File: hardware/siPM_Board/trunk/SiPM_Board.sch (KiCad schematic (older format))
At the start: 25 parts, among them J1 Conn_02x34_Odd_Even, J2 Conn_02x34_Odd_Even, U1 LM94021, U2 S14161-6050HS-04, U3 S14161-6050HS-04, U4 S14161-6050HS-04, U5 S14161-6050HS-04

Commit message: All footprints are made
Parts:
- J1, J2: footprint Connector_Samtec_HLE_SMD:Samtec_HLE-134-02-xxx-DV-BE-A_2x34_P2.54mm_Horizontal -> Arich_SiPM_Footprints:MW-34-03-G-D-245-065-ES
- U1: footprint (none) -> Arich_SiPM_Footprints:Texas_R-PDSO-G6
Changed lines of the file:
@@
 F 0 "U1" H 2150 4085 50  0000 C CNN
 F 1 "LM94021" H 2150 4176 50  0000 C CNN
-F 2 "" H 2195 4473 50  0001 C CNN
+F 2 "Arich_SiPM_Footprints:Texas_R-PDSO-G6" H 2195 4473 50  0001 C CNN
 F 3 "https://www.ti.com/lit/ds/symlink/lm94021.pdf?ts=1612369710364&ref_url=https%253A%252F%252Fwww.ti.com%252Fproduct%252FLM94021" H 2195 4473 50  0001 C CNN
 	1    2150 4650
@@
 F 0 "J1" H 5650 1525 50  0000 R CNN
 F 1 "Conn_02x34_Odd_Even" H 6400 1650 50  0000 R CNN
-F 2 "Connector_Samtec_HLE_SMD:Samtec_HLE-134-02-xxx-DV-BE-A_2x34_P2.54mm_Horizontal" H 6000 3550 50  0001 C CNN
+F 2 "Arich_SiPM_Footprints:MW-34-03-G-D-245-065-ES" H 6000 3550 50  0001 C CNN
 F 3 "~" H 6000 3550 50  0001 C CNN
 	1    6000 3550
@@
 F 0 "J2" H 8975 1525 50  0000 R CNN
 F 1 "Conn_02x34_Odd_Even" H 9750 1650 50  0000 R CNN
-F 2 "Connector_Samtec_HLE_SMD:Samtec_HLE-134-02-xxx-DV-BE-A_2x34_P2.54mm_Horizontal" H 9350 3550 50  0001 C CNN
+F 2 "Arich_SiPM_Footprints:MW-34-03-G-D-245-065-ES" H 9350 3550 50  0001 C CNN
 F 3 "~" H 9350 3550 50  0001 C CNN
 	1    9350 3550

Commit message: Layout Needs Editing
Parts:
- C1, C10, C11, C12, C13, C14, C15, C16, C17, C18, C2, C3, C4, C5, C6, C7, C8, C9: footprint Capacitor_SMD:C_1206_3216Metric_Pad1.33x1.80mm_HandSolder -> Capacitor_SMD:C_0603_1608Metric_Pad1.08x0.95mm_HandSolder; Item Cost $0.85 -> $0.12; MFN C3216C0G2A104J160AC -> 0603B104K101CT; Supplier P/N 445-172677-1-ND -> 1292-1392-1-ND

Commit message: Schematic changes made
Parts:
- removed C10, C11, C14, C15, C16, C5, C6, C9: 100nF, Capacitor_SMD:C_0603_1608Metric_Pad1.08x0.95mm_HandSolder, symbol Device:C
- renumbered C18 to C10, C12 to C5, C13 to C6, C17 to C9
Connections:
- net BIAS1: now also J1.2 (Pin_2); no longer C3.1, C4.1, C7.1, C8.1, J1.67 (Pin_67), J1.68 (Pin_68), U3.B1 (A1K), U3.B3 (A2K), U3.B5 (A3K), U3.B7 (A4K), U3.D1 (B1K), U3.D3 (B2K), U3.D5 (B3K), U3.D7 (B4K), U3.F2 (C1K), U3.F4 (C2K), U3.F6 (C3K), U3.F8 (C4K), U3.H2 (D1K), U3.H4 (D2K), U3.H6 (D3K), U3.H8 (D4K)
- net BIAS2: now also C3.1, C4.1, J1.67 (Pin_67), U3.B1 (A1K), U3.B3 (A2K), U3.B5 (A3K), U3.B7 (A4K), U3.D1 (B1K), U3.D3 (B2K), U3.D5 (B3K), U3.D7 (B4K), U3.F2 (C1K), U3.F4 (C2K), U3.F6 (C3K), U3.F8 (C4K), U3.H2 (D1K), U3.H4 (D2K), U3.H6 (D3K), U3.H8 (D4K); no longer C5.1, C6.1, J2.67 (Pin_67), J2.68 (Pin_68), U4.B1 (A1K), U4.B3 (A2K), U4.B5 (A3K), U4.B7 (A4K), U4.D1 (B1K), U4.D3 (B2K), U4.D5 (B3K), U4.D7 (B4K), U4.F2 (C1K), U4.F4 (C2K), U4.F6 (C3K), U4.F8 (C4K), U4.H2 (D1K), U4.H4 (D2K), U4.H6 (D3K), U4.H8 (D4K), U5.B1 (A1K), U5.B3 (A2K), U5.B5 (A3K), U5.B7 (A4K), U5.D1 (B1K), U5.D3 (B2K), U5.D5 (B3K), U5.D7 (B4K), U5.F2 (C1K), U5.F4 (C2K), U5.F6 (C3K), U5.F8 (C4K), U5.H2 (D1K), U5.H4 (D2K), U5.H6 (D3K), U5.H8 (D4K)
- net GND: now also J1.66 (Pin_66), J2.66 (Pin_66); no longer C7.2, C8.2, J1.2 (Pin_2), J2.2 (Pin_2)
- net OUT: now also J1.68 (Pin_68); no longer J1.66 (Pin_66)
- new net: C7.2, C8.2
- new net BIAS3: C5.1, C6.1, J2.2 (Pin_2), U4.B1 (A1K), U4.B3 (A2K), U4.B5 (A3K), U4.B7 (A4K), U4.D1 (B1K), U4.D3 (B2K), U4.D5 (B3K), U4.D7 (B4K), U4.F2 (C1K), U4.F4 (C2K), U4.F6 (C3K), U4.F8 (C4K), U4.H2 (D1K), U4.H4 (D2K), U4.H6 (D3K), U4.H8 (D4K)
- new net BIAS4: C7.1, C8.1, J2.67 (Pin_67), J2.68 (Pin_68), U5.B1 (A1K), U5.B3 (A2K), U5.B5 (A3K), U5.B7 (A4K), U5.D1 (B1K), U5.D3 (B2K), U5.D5 (B3K), U5.D7 (B4K), U5.F2 (C1K), U5.F4 (C2K), U5.F6 (C3K), U5.F8 (C4K), U5.H2 (D1K), U5.H4 (D2K), U5.H6 (D3K), U5.H8 (D4K)
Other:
- moved on the sheet: C10, C5, C6, C9, J1, J2, U1, U2, U3, U4, U5

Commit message: Tracing incomplete
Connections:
- net GND: now also C7.2, C8.2
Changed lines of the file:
@@
 Text Label 9850 1850 2    50   ~ 0
 BIAS3
+$Comp
+L power:GND #PWR?
+U 1 1 602B2E79
+P 6550 4150
+F 0 "#PWR?" H 6550 3900 50  0001 C CNN
+F 1 "GND" H 6555 3977 50  0000 C CNN
+F 2 "" H 6550 4150 50  0001 C CNN
+F 3 "" H 6550 4150 50  0001 C CNN
+	1    6550 4150
+	1    0    0    -1
+$EndComp
 $EndSCHEMATC

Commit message: Tracing incomplete
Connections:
- net BIAS2: now also J1.68 (Pin_68); no longer J1.67 (Pin_67)
- net OUT: now also J1.67 (Pin_67); no longer J1.68 (Pin_68)
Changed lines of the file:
@@
 Wire Wire Line
 	7800 5900 8650 5900
-Text Label 5350 5150 0    50   ~ 0
+Text Label 4750 5150 2    50   ~ 0
 OUT
 Wire Wire Line
@@
 Text Label 4750 5050 2    50   ~ 0
 VDD
-Wire Wire Line
-	4800 5150 4550 5150
-Text Label 4550 5150 0    50   ~ 0
+Text Label 5350 5150 0    50   ~ 0
 BIAS2
 Wire Wire Line
@@
 	2050 4000 2050 3950
 $Comp
-L power:GND #PWR?
+L power:GND #PWR0101
 U 1 1 60DAF09E
 P 2200 4100
-F 0 "#PWR?" H 2200 3850 50  0001 C CNN
+F 0 "#PWR0101" H 2200 3850 50  0001 C CNN
 F 1 "GND" H 2205 3927 50  0000 C CNN
 F 2 "" H 2200 4100 50  0001 C CNN
@@
 	2050 1300 2050 1250
 $Comp
-L power:GND #PWR?
+L power:GND #PWR0102
 U 1 1 60F1D723
 P 2200 1400
-F 0 "#PWR?" H 2200 1150 50  0001 C CNN
+F 0 "#PWR0102" H 2200 1150 50  0001 C CNN
 F 1 "GND" H 2205 1227 50  0000 C CNN
 F 2 "" H 2200 1400 50  0001 C CNN
@@
 BIAS3
 $Comp
-L power:GND #PWR?
+L power:GND #PWR0103
 U 1 1 602B2E79
 P 6550 4150
-F 0 "#PWR?" H 6550 3900 50  0001 C CNN
+F 0 "#PWR0103" H 6550 3900 50  0001 C CNN
 F 1 "GND" H 6555 3977 50  0000 C CNN
 F 2 "" H 6550 4150 50  0001 C CNN
@@
 	1    0    0    -1
 $EndComp
+Wire Wire Line
+	4800 5150 4750 5150
 $EndSCHEMATC

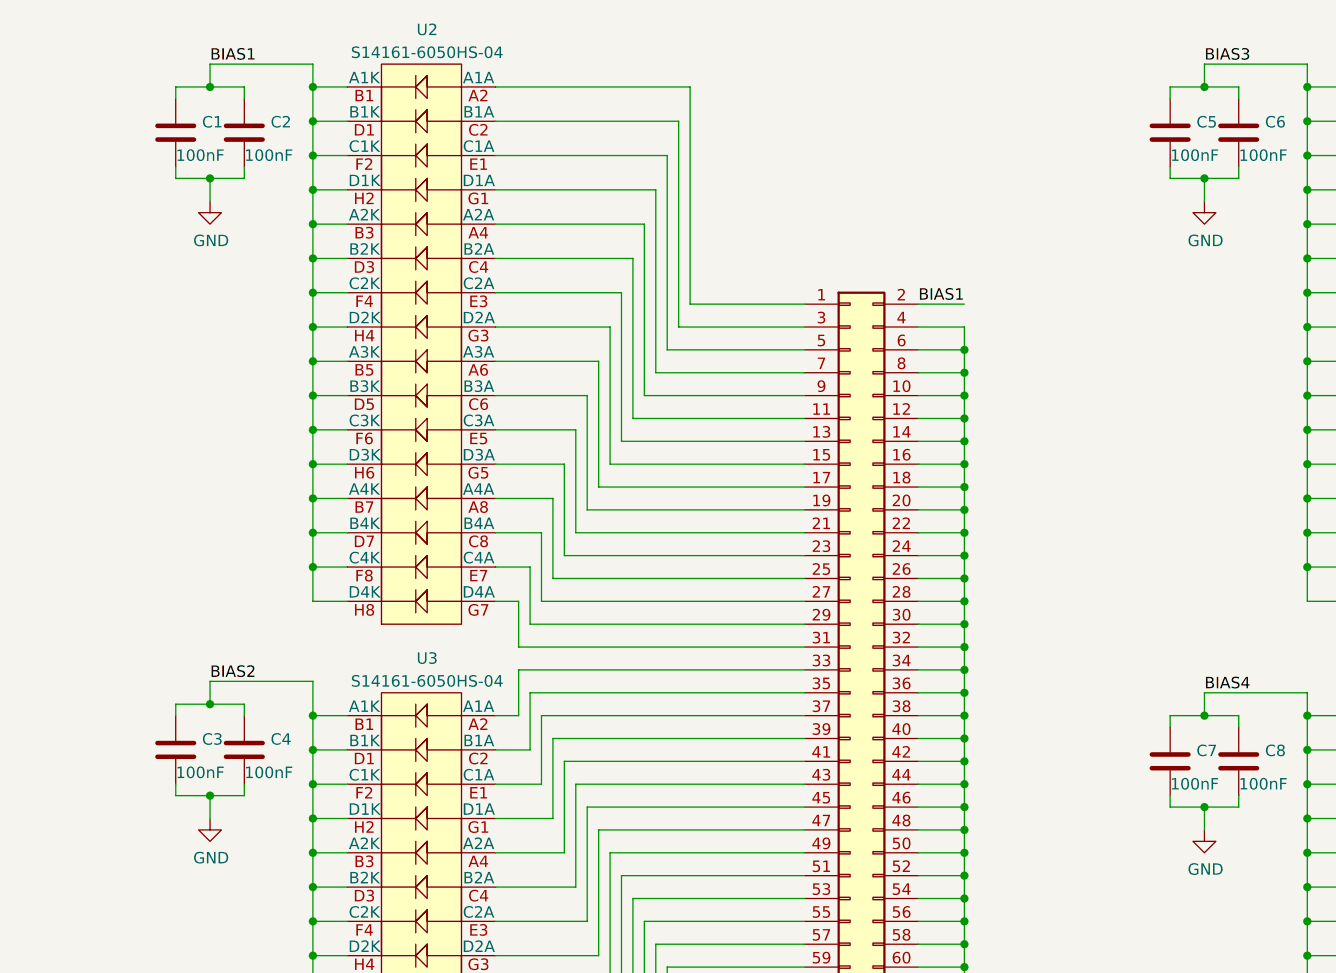
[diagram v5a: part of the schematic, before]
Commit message: Annotaed extra capacitors
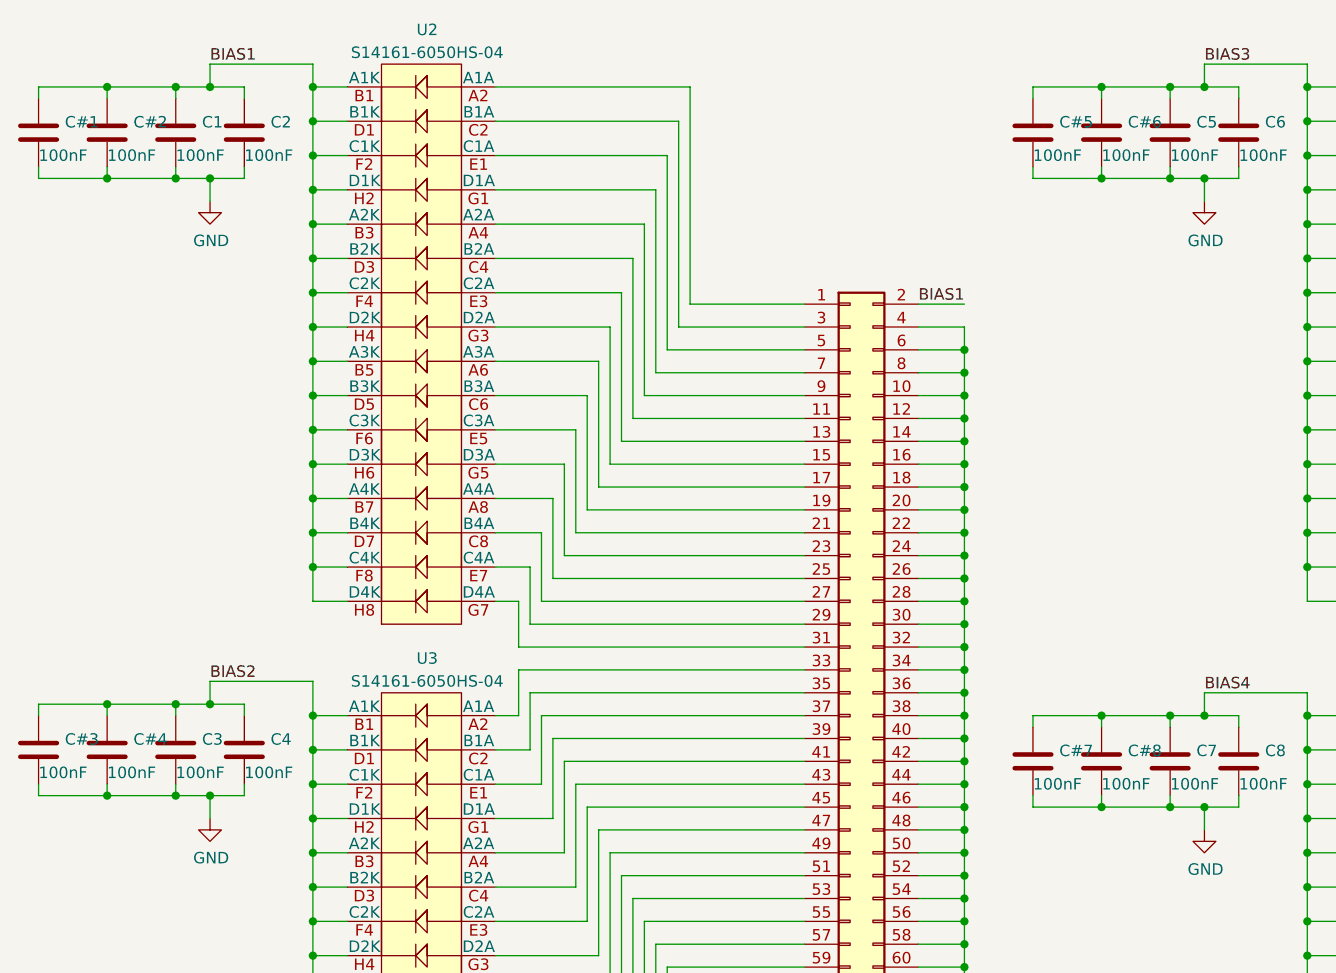
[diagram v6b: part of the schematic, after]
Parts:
- added C#1, C#2, C#3, C#4, C#5, C#6, C#7, C#8: 100nF, Capacitor_SMD:C_0603_1608Metric_Pad1.08x0.95mm_HandSolder, symbol Device:C
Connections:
- net BIAS1: now also C#1.1, C#2.1
- net BIAS2: now also C#3.1, C#4.1
- net BIAS3: now also C#5.1, C#6.1
- net BIAS4: now also C#7.1, C#8.1
- net GND: now also C#1.2, C#2.2, C#3.2, C#4.2, C#5.2, C#6.2, C#7.2, C#8.2

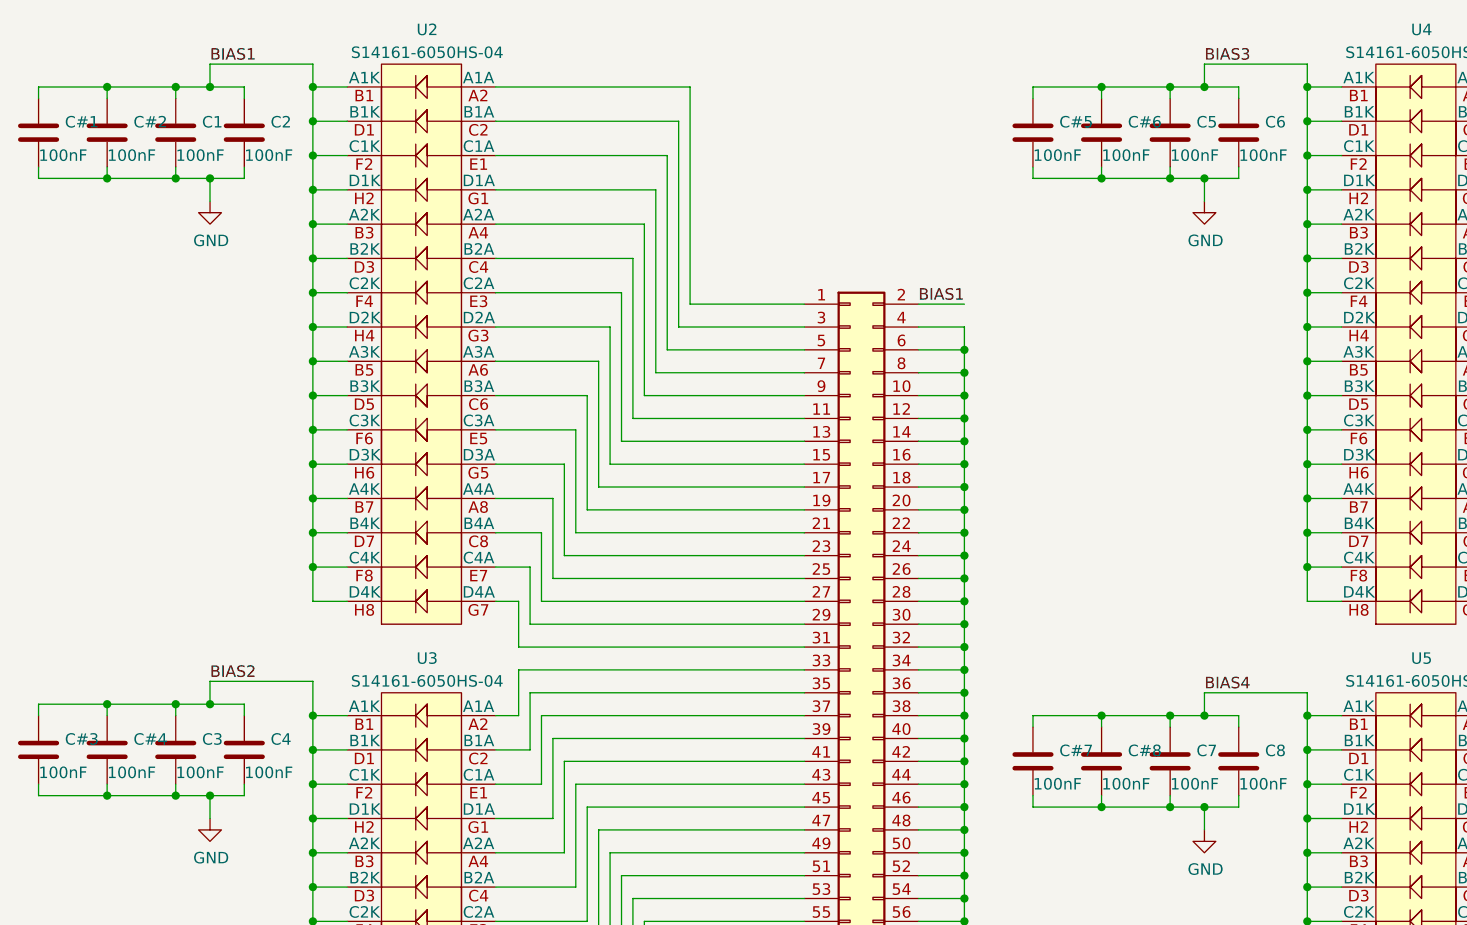
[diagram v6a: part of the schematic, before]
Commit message: Schematic reference updates
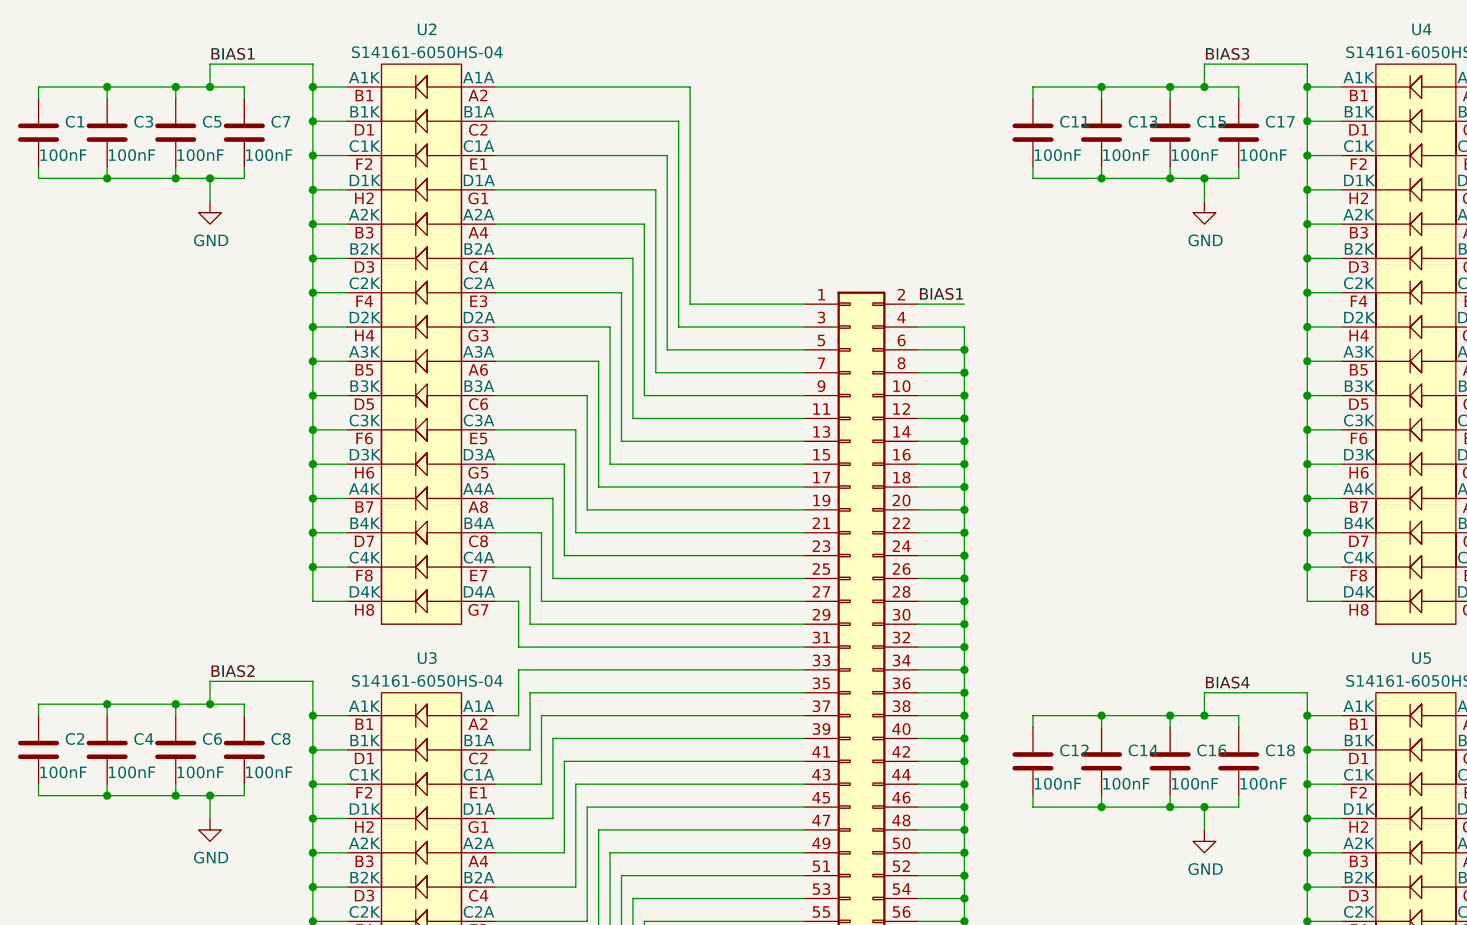
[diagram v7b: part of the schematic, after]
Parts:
- renumbered C#1 to C1, C#5 to C11, C#7 to C12, C#6 to C13, C#8 to C14, C5 to C15, C7 to C16, C6 to C17, C8 to C18, C#3 to C2, C#2 to C3, C#4 to C4, C1 to C5, C3 to C6, C2 to C7, C4 to C8
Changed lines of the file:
@@
 Connection ~ 9850 2050
 $Comp
-L power:GND #PWR05
+L power:GND #PWR07
 U 1 1 61207A7A
 P 9850 5250
-F 0 "#PWR05" H 9850 5000 50  0001 C CNN
+F 0 "#PWR07" H 9850 5000 50  0001 C CNN
 F 1 "GND" H 9855 5077 50  0000 C CNN
 F 2 "" H 9850 5250 50  0001 C CNN
@@
 OUT
 $Comp
-L Device:C C6
+L Device:C C17
 U 1 1 604DBA71
 P 6700 1100
-F 0 "C6" H 6815 1146 50  0000 L CNN
+F 0 "C17" H 6815 1146 50  0000 L CNN
 F 1 "100nF" H 6700 1000 50  0000 L CNN
 F 2 "Capacitor_SMD:C_0603_1608Metric_Pad1.08x0.95mm_HandSolder" H 6738 950 50  0001 C CNN
@@
 $EndComp
 $Comp
-L Device:C C5
+L Device:C C15
 U 1 1 604DBA63
 P 6400 1100
-F 0 "C5" H 6515 1146 50  0000 L CNN
+F 0 "C15" H 6515 1146 50  0000 L CNN
 F 1 "100nF" H 6400 1000 50  0000 L CNN
 F 2 "Capacitor_SMD:C_0603_1608Metric_Pad1.08x0.95mm_HandSolder" H 6438 950 50  0001 C CNN
@@
 	6400 1300 6400 1250
 $Comp
-L power:GND #PWR02
+L power:GND #PWR05
 U 1 1 6023C2FA
 P 6550 1400
-F 0 "#PWR02" H 6550 1150 50  0001 C CNN
+F 0 "#PWR05" H 6550 1150 50  0001 C CNN
 F 1 "GND" H 6555 1227 50  0000 C CNN
 F 2 "" H 6550 1400 50  0001 C CNN
@@
 BIAS2
 $Comp
-L Device:C C4
+L Device:C C8
 U 1 1 60DAF07F
 P 2350 3800
-F 0 "C4" H 2465 3846 50  0000 L CNN
+F 0 "C8" H 2465 3846 50  0000 L CNN
 F 1 "100nF" H 2350 3700 50  0000 L CNN
 F 2 "Capacitor_SMD:C_0603_1608Metric_Pad1.08x0.95mm_HandSolder" H 2388 3650 50  0001 C CNN
@@
 $EndComp
 $Comp
-L Device:C C3
+L Device:C C6
 U 1 1 60DAF08D
 P 2050 3800
-F 0 "C3" H 2165 3846 50  0000 L CNN
+F 0 "C6" H 2165 3846 50  0000 L CNN
 F 1 "100nF" H 2050 3700 50  0000 L CNN
 F 2 "Capacitor_SMD:C_0603_1608Metric_Pad1.08x0.95mm_HandSolder" H 2088 3650 50  0001 C CNN
@@
 	2050 4000 2050 3950
 $Comp
-L power:GND #PWR0101
+L power:GND #PWR02
 U 1 1 60DAF09E
 P 2200 4100
-F 0 "#PWR0101" H 2200 3850 50  0001 C CNN
+F 0 "#PWR02" H 2200 3850 50  0001 C CNN
 F 1 "GND" H 2205 3927 50  0000 C CNN
 F 2 "" H 2200 4100 50  0001 C CNN
@@
 	2050 1300 2050 1250
 $Comp
-L power:GND #PWR0102
+L power:GND #PWR01
 U 1 1 60F1D723
 P 2200 1400
-F 0 "#PWR0102" H 2200 1150 50  0001 C CNN
+F 0 "#PWR01" H 2200 1150 50  0001 C CNN
 F 1 "GND" H 2205 1227 50  0000 C CNN
 F 2 "" H 2200 1400 50  0001 C CNN
@@
 BIAS4
 $Comp
-L Device:C C8
+L Device:C C18
 U 1 1 60F797D1
 P 6700 3850
-F 0 "C8" H 6815 3896 50  0000 L CNN
+F 0 "C18" H 6815 3896 50  0000 L CNN
 F 1 "100nF" H 6700 3750 50  0000 L CNN
 F 2 "Capacitor_SMD:C_0603_1608Metric_Pad1.08x0.95mm_HandSolder" H 6738 3700 50  0001 C CNN
@@
 $EndComp
 $Comp
-L Device:C C7
+L Device:C C16
 U 1 1 60F797DF
 P 6400 3850
-F 0 "C7" H 6515 3896 50  0000 L CNN
+F 0 "C16" H 6515 3896 50  0000 L CNN
 F 1 "100nF" H 6400 3750 50  0000 L CNN
 F 2 "Capacitor_SMD:C_0603_1608Metric_Pad1.08x0.95mm_HandSolder" H 6438 3700 50  0001 C CNN
@@
 BIAS3
 $Comp
-L power:GND #PWR0103
+L power:GND #PWR06
 U 1 1 602B2E79
 P 6550 4150
-F 0 "#PWR0103" H 6550 3900 50  0001 C CNN
+F 0 "#PWR06" H 6550 3900 50  0001 C CNN
 F 1 "GND" H 6555 3977 50  0000 C CNN
 F 2 "" H 6550 4150 50  0001 C CNN
@@
 	4800 5150 4750 5150
 $Comp
-L Device:C C#2
+L Device:C C3
 U 1 1 60372068
 P 1750 1100
-F 0 "C#2" H 1865 1146 50  0000 L CNN
+F 0 "C3" H 1865 1146 50  0000 L CNN
 F 1 "100nF" H 1750 1000 50  0000 L CNN
 F 2 "Capacitor_SMD:C_0603_1608Metric_Pad1.08x0.95mm_HandSolder" H 1788 950 50  0001 C CNN
@@
 $EndComp
 $Comp
-L Device:C C#1
+L Device:C C1
 U 1 1 6037BC42
 P 1450 1100
-F 0 "C#1" H 1565 1146 50  0000 L CNN
+F 0 "C1" H 1565 1146 50  0000 L CNN
 F 1 "100nF" H 1450 1000 50  0000 L CNN
 F 2 "Capacitor_SMD:C_0603_1608Metric_Pad1.08x0.95mm_HandSolder" H 1488 950 50  0001 C CNN
@@
 $EndComp
 $Comp
-L Device:C C#4
+L Device:C C4
 U 1 1 6037EBF4
 P 1750 3800
-F 0 "C#4" H 1865 3846 50  0000 L CNN
+F 0 "C4" H 1865 3846 50  0000 L CNN
 F 1 "100nF" H 1750 3700 50  0000 L CNN
 F 2 "Capacitor_SMD:C_0603_1608Metric_Pad1.08x0.95mm_HandSolder" H 1788 3650 50  0001 C CNN
@@
 $EndComp
 $Comp
-L Device:C C#3
+L Device:C C2
 U 1 1 6037EC10
 P 1450 3800
-F 0 "C#3" H 1565 3846 50  0000 L CNN
+F 0 "C2" H 1565 3846 50  0000 L CNN
 F 1 "100nF" H 1450 3700 50  0000 L CNN
 F 2 "Capacitor_SMD:C_0603_1608Metric_Pad1.08x0.95mm_HandSolder" H 1488 3650 50  0001 C CNN
@@
 $EndComp
 $Comp
-L Device:C C#8
+L Device:C C14
 U 1 1 603C9FC8
 P 6100 3850
-F 0 "C#8" H 6215 3896 50  0000 L CNN
+F 0 "C14" H 6215 3896 50  0000 L CNN
 F 1 "100nF" H 6100 3750 50  0000 L CNN
 F 2 "Capacitor_SMD:C_0603_1608Metric_Pad1.08x0.95mm_HandSolder" H 6138 3700 50  0001 C CNN
@@
 $EndComp
 $Comp
-L Device:C C#7
+L Device:C C12
 U 1 1 603C9FE4
 P 5800 3850
-F 0 "C#7" H 5915 3896 50  0000 L CNN
+F 0 "C12" H 5915 3896 50  0000 L CNN
 F 1 "100nF" H 5800 3750 50  0000 L CNN
 F 2 "Capacitor_SMD:C_0603_1608Metric_Pad1.08x0.95mm_HandSolder" H 5838 3700 50  0001 C CNN
@@
 $EndComp
 $Comp
-L Device:C C#6
+L Device:C C13
 U 1 1 60413ED0
 P 6100 1100
-F 0 "C#6" H 6215 1146 50  0000 L CNN
+F 0 "C13" H 6215 1146 50  0000 L CNN
 F 1 "100nF" H 6100 1000 50  0000 L CNN
 F 2 "Capacitor_SMD:C_0603_1608Metric_Pad1.08x0.95mm_HandSolder" H 6138 950 50  0001 C CNN
@@
 $EndComp
 $Comp
-L Device:C C#5
+L Device:C C11
 U 1 1 60413EDE
 P 5800 1100
-F 0 "C#5" H 5915 1146 50  0000 L CNN
+F 0 "C11" H 5915 1146 50  0000 L CNN
 F 1 "100nF" H 5800 1000 50  0000 L CNN
 F 2 "Capacitor_SMD:C_0603_1608Metric_Pad1.08x0.95mm_HandSolder" H 5838 950 50  0001 C CNN
@@
 $EndComp
 $Comp
-L Device:C C1
+L Device:C C5
 U 1 1 60F1D712
 P 2050 1100
-F 0 "C1" H 2165 1146 50  0000 L CNN
+F 0 "C5" H 2165 1146 50  0000 L CNN
 F 1 "100nF" H 2050 1000 50  0000 L CNN
 F 2 "Capacitor_SMD:C_0603_1608Metric_Pad1.08x0.95mm_HandSolder" H 2088 950 50  0001 C CNN
@@
 $EndComp
 $Comp
-L Device:C C2
+L Device:C C7
 U 1 1 60F1D704
 P 2350 1100
-F 0 "C2" H 2465 1146 50  0000 L CNN
+F 0 "C7" H 2465 1146 50  0000 L CNN
 F 1 "100nF" H 2350 1000 50  0000 L CNN
 F 2 "Capacitor_SMD:C_0603_1608Metric_Pad1.08x0.95mm_HandSolder" H 2388 950 50  0001 C CNN
